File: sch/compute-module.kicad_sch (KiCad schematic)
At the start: 10 parts, among them J2 SAM10346-ND, J3 Conn_02x20_Odd_Even, M1 ComputeModule5-CM5, SW1 1825910-6

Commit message: pågebynt merging av pwr-supply og modem branches
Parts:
- renumbered C18 to C3, C19 to C4, C17 to C5, D5 to D1, J2 to J3, J3 to J4
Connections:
- net +3V3 is gone; now on net +3V3_CM5: J4.1 (Pin_1)
- net PCIE_nCLKREQ: now reaches M1.102 (PCIe_nCLKREQ)
- net PCIE_nWAKE: now reaches M1.104 (PCIE_nWAKE)
- net PCIE_PWR_EN: now reaches M1.106 (PCIE_PWR_EN)
- net PCIE_nRST: now reaches M1.109 (PCIe_nRST)
- net PCIE_CLK_P: now reaches M1.110 (PCIe_CLK_P)
- net PCIE_CLK_N: now reaches M1.112 (PCIe_CLK_N)
- net PCIE_RX_P: now reaches M1.116 (PCIe_RX_P)
- net PCIE_RX_N: now reaches M1.118 (PCIe_RX_N)
- net PCIE_TX_P: now reaches M1.122 (PCIe_TX_P)
- net PCIE_TX_N: now reaches M1.124 (PCIe_TX_N)
- no-connect marks 119 -> 109
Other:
- note added: "FLASH / BMS USB"
- note added: "MODEM USB"
- note added: "SD USB"
- moved on the sheet: BT1, C3, C4, C5, D1, J3, J4, R2, SW1

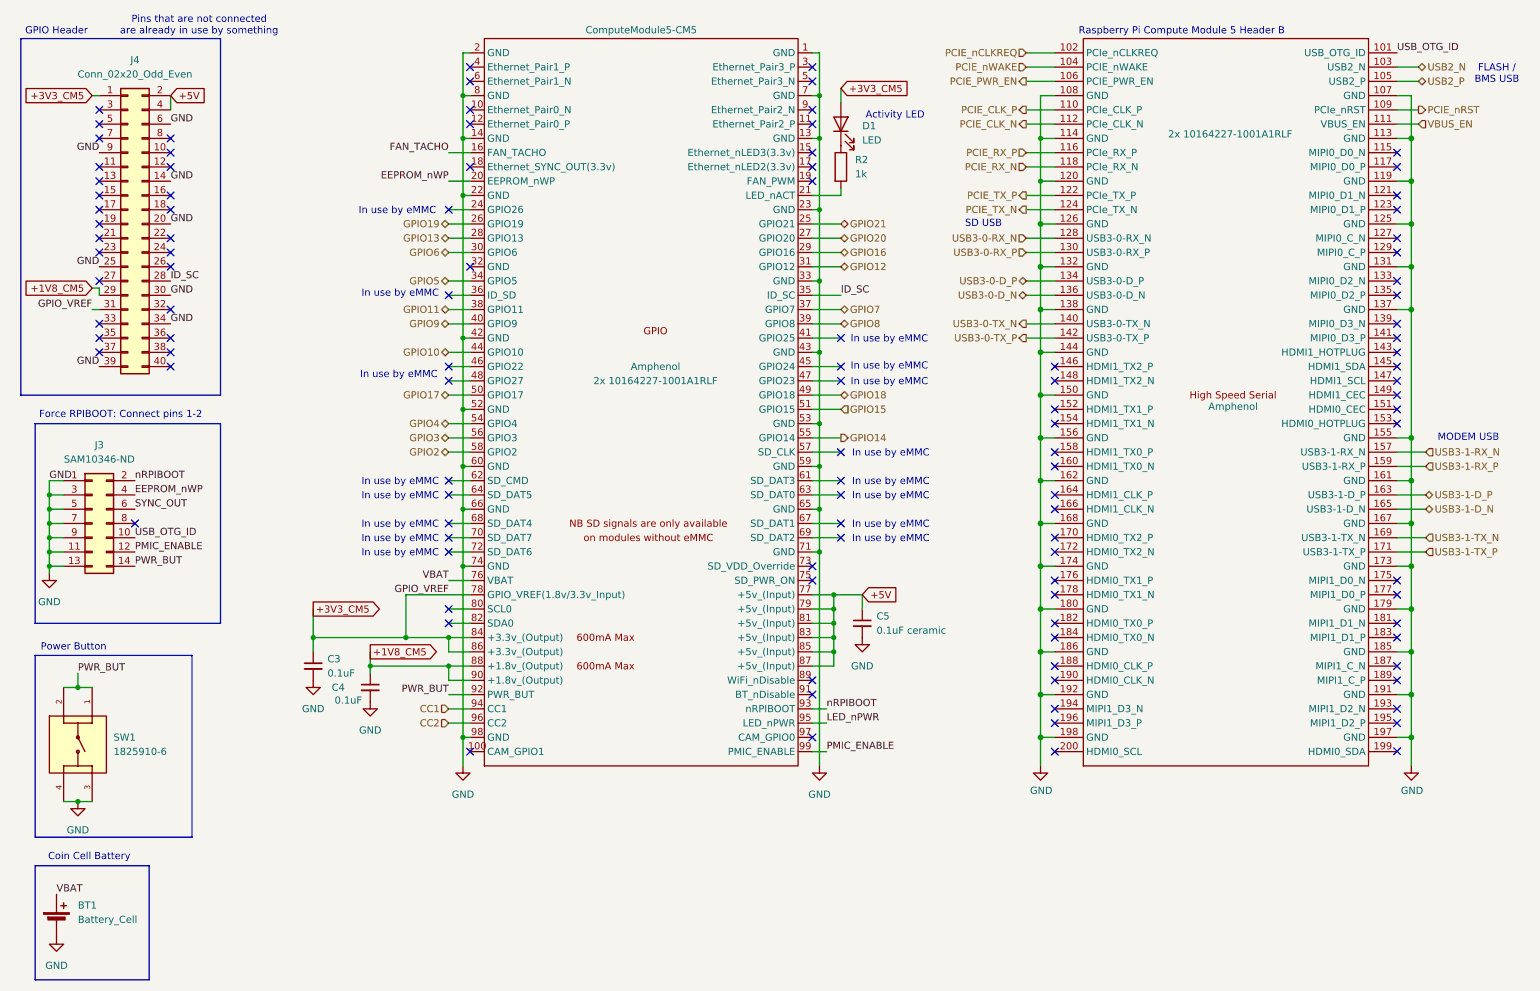
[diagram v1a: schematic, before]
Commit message: lagt inn footprint på alt, obs feil footprint i pwr-supply
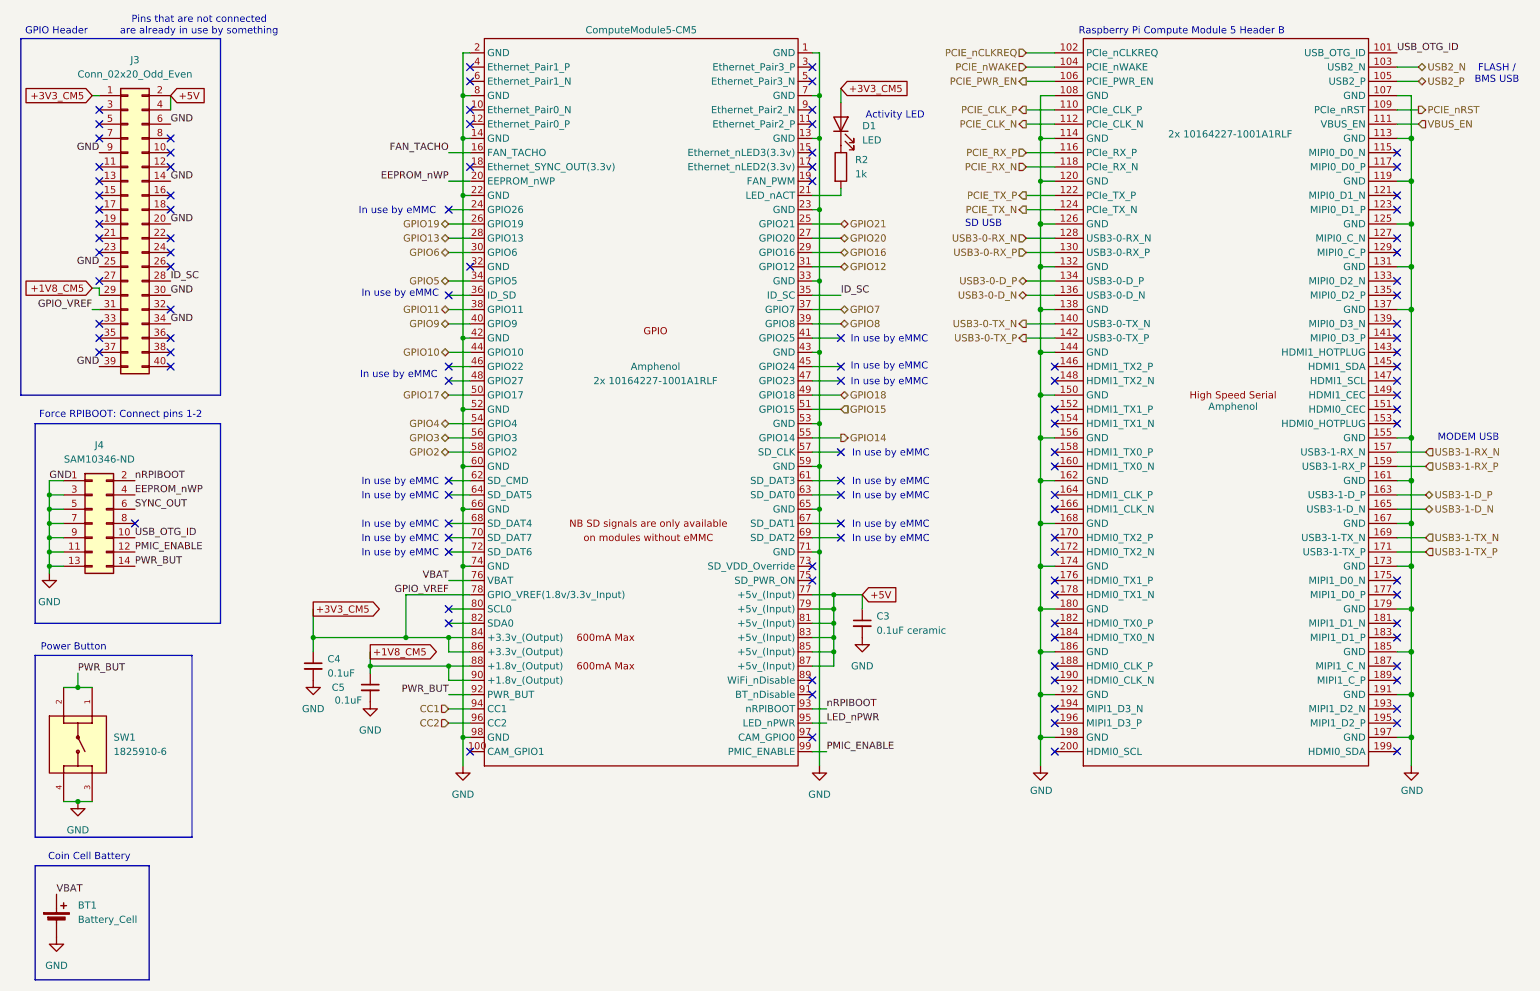
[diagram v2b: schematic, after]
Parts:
- renumbered C5 to C3, C3 to C4, C4 to C5, J4 to J3, J3 to J4
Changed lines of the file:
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@@
 		(on_board yes)
 		(dnp no)
-		(property "Reference" "#PWR017"
+		(property "Reference" "#PWR015"
 			(at 264.16 158.75 0)
 			(effects
@@
 			(project "audiograb"
 				(path "/c46c2311-6d4b-411d-b012-c7730eac136d/980eb6bd-3c2d-40a6-a375-772dc2df4153"
-					(reference "#PWR017")
+					(reference "#PWR015")
 					(unit 1)
 				)
@@
 		(on_board yes)
 		(dnp no)
-		(property "Reference" "#PWR016"
+		(property "Reference" "#PWR014"
 			(at 198.12 158.75 0)
 			(effects
@@
 			(project "audiograb"
 				(path "/c46c2311-6d4b-411d-b012-c7730eac136d/980eb6bd-3c2d-40a6-a375-772dc2df4153"
-					(reference "#PWR016")
+					(reference "#PWR014")
 					(unit 1)
 				)
@@
 		(dnp no)
 		(fields_autoplaced yes)
-		(property "Reference" "#PWR015"
+		(property "Reference" "#PWR09"
 			(at 166.37 135.89 0)
 			(effects
@@
 			(project "audiograb"
 				(path "/c46c2311-6d4b-411d-b012-c7730eac136d/980eb6bd-3c2d-40a6-a375-772dc2df4153"
-					(reference "#PWR015")
+					(reference "#PWR09")
 					(unit 1)
 				)
@@
 		(dnp no)
 		(fields_autoplaced yes)
-		(property "Reference" "J4"
+		(property "Reference" "J3"
 			(at 36.83 26.67 0)
 			(effects
@@
 			(project "audiograb"
 				(path "/c46c2311-6d4b-411d-b012-c7730eac136d/980eb6bd-3c2d-40a6-a375-772dc2df4153"
-					(reference "J4")
+					(reference "J3")
 					(unit 1)
 				)
@@
 		(on_board yes)
 		(dnp no)
-		(property "Reference" "#PWR013"
+		(property "Reference" "#PWR012"
 			(at 95.25 158.75 0)
 			(effects
@@
 			(project "audiograb"
 				(path "/c46c2311-6d4b-411d-b012-c7730eac136d/980eb6bd-3c2d-40a6-a375-772dc2df4153"
-					(reference "#PWR013")
+					(reference "#PWR012")
 					(unit 1)
 				)
@@
 		(dnp no)
 		(fields_autoplaced yes)
-		(property "Reference" "#PWR09"
+		(property "Reference" "#PWR017"
 			(at 22.86 189.23 0)
 			(effects
@@
 			(project "audiograb"
 				(path "/c46c2311-6d4b-411d-b012-c7730eac136d/980eb6bd-3c2d-40a6-a375-772dc2df4153"
-					(reference "#PWR09")
+					(reference "#PWR017")
 					(unit 1)
 				)
@@
 		(dnp no)
 		(fields_autoplaced yes)
-		(property "Reference" "#PWR011"
+		(property "Reference" "#PWR010"
 			(at 68.58 143.51 0)
 			(effects
@@
 			(project "audiograb"
 				(path "/c46c2311-6d4b-411d-b012-c7730eac136d/980eb6bd-3c2d-40a6-a375-772dc2df4153"
-					(reference "#PWR011")
+					(reference "#PWR010")
 					(unit 1)
 				)
@@
 		(dnp no)
 		(fields_autoplaced yes)
-		(property "Reference" "C3"
+		(property "Reference" "C4"
 			(at 71.12 133.3562 0)
 			(effects
@@
 			(project "audiograb"
 				(path "/c46c2311-6d4b-411d-b012-c7730eac136d/980eb6bd-3c2d-40a6-a375-772dc2df4153"
-					(reference "C3")
+					(reference "C4")
 					(unit 1)
 				)
@@
 		(dnp no)
 		(fields_autoplaced yes)
-		(property "Reference" "#PWR012"
+		(property "Reference" "#PWR011"
 			(at 78.74 147.32 0)
 			(effects
@@
 			(project "audiograb"
 				(path "/c46c2311-6d4b-411d-b012-c7730eac136d/980eb6bd-3c2d-40a6-a375-772dc2df4153"
-					(reference "#PWR012")
+					(reference "#PWR011")
 					(unit 1)
 				)
@@
 		(dnp no)
 		(fields_autoplaced yes)
-		(property "Reference" "C5"
+		(property "Reference" "C3"
 			(at 168.91 125.7362 0)
 			(effects
@@
 			(project "audiograb"
 				(path "/c46c2311-6d4b-411d-b012-c7730eac136d/980eb6bd-3c2d-40a6-a375-772dc2df4153"
-					(reference "C5")
+					(reference "C3")
 					(unit 1)
 				)
@@
 		(dnp no)
 		(fields_autoplaced yes)
-		(property "Reference" "J3"
+		(property "Reference" "J4"
 			(at 30.48 95.25 0)
 			(effects
@@
 			(project "audiograb"
 				(path "/c46c2311-6d4b-411d-b012-c7730eac136d/980eb6bd-3c2d-40a6-a375-772dc2df4153"
-					(reference "J3")
+					(reference "J4")
 					(unit 1)
 				)
@@
 		(dnp no)
 		(fields_autoplaced yes)
-		(property "Reference" "#PWR014"
+		(property "Reference" "#PWR013"
 			(at 158.75 158.75 0)
 			(effects
@@
 			(project "audiograb"
 				(path "/c46c2311-6d4b-411d-b012-c7730eac136d/980eb6bd-3c2d-40a6-a375-772dc2df4153"
-					(reference "#PWR014")
+					(reference "#PWR013")
 					(unit 1)
 				)
@@
 		(dnp no)
 		(fields_autoplaced yes)
-		(property "Reference" "#PWR010"
+		(property "Reference" "#PWR016"
 			(at 26.67 165.1 0)
 			(effects
@@
 			(project "audiograb"
 				(path "/c46c2311-6d4b-411d-b012-c7730eac136d/980eb6bd-3c2d-40a6-a375-772dc2df4153"
-					(reference "#PWR010")
+					(reference "#PWR016")
 					(unit 1)
 				)
@@
 		(on_board yes)
 		(dnp no)
-		(property "Reference" "C4"
+		(property "Reference" "C5"
 			(at 71.882 138.43 0)
 			(effects
@@
 			(project "audiograb"
 				(path "/c46c2311-6d4b-411d-b012-c7730eac136d/980eb6bd-3c2d-40a6-a375-772dc2df4153"
-					(reference "C4")
+					(reference "C5")
 					(unit 1)
 				)

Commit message: Fjernet gammelt og la til nye komponenter, merging ferdig
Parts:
- removed BT1: Battery_Cell, Battery:BatteryHolder_Keystone_3034_1x20mm, symbol Device:Battery_Cell
- renumbered C3 to C17, C4 to C18, C5 to C19, D1 to D5, J4 to J2
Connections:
- net VBAT is gone; now on net +3V3_CM5: M1.76 (VBAT)
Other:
- note removed: "Coin Cell Battery"
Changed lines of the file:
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@@
 		)
 	)
-	(rectangle
-		(start 19.05 170.18)
-		(end 39.37 190.5)
-		(stroke
-			(width 0)
-			(type default)
-		)
-		(fill
-			(type none)
-		)
-	)
 	(text "In use by eMMC"
 		(exclude_from_sim no)
@@
 		)
 	)
-	(text "Coin Cell Battery"
-		(exclude_from_sim no)
-		(at 28.702 168.656 0)
-		(effects
-			(font
-				(size 1.27 1.27)
-			)
-		)
-	)
 	(text "Power Button\n"
 		(exclude_from_sim no)
@@
 	(wire
 		(pts
+			(xy 93.98 119.38) (xy 96.52 119.38)
+		)
+		(stroke
+			(width 0)
+			(type default)
+		)
+	)
+	(wire
+		(pts
 			(xy 198.12 109.22) (xy 198.12 116.84)
 		)
@@
 	(wire
 		(pts
+			(xy 93.98 118.11) (xy 93.98 119.38)
+		)
+		(stroke
+			(width 0)
+			(type default)
+		)
+	)
+	(wire
+		(pts
 			(xy 264.16 147.32) (xy 264.16 152.4)
 		)
@@
 	(wire
 		(pts
-			(xy 92.71 119.38) (xy 96.52 119.38)
+			(xy 90.17 118.11) (xy 93.98 118.11)
 		)
 		(stroke
@@
 		)
 	)
-	(label "VBAT"
-		(at 92.71 119.38 180)
-		(effects
-			(font
-				(size 1.27 1.27)
-			)
-			(justify right bottom)
-		)
-	)
 	(label "PMIC_ENABLE"
 		(at 36.83 114.3 0)
@@
 		)
 	)
-	(label "VBAT"
-		(at 22.86 175.26 0)
-		(effects
-			(font
-				(size 1.27 1.27)
-			)
-			(justify left bottom)
-		)
-	)
 	(label "GPIO_VREF"
 		(at 29.21 71.12 180)
@@
 	)
 	(global_label "+3V3_CM5"
+		(shape input)
+		(at 90.17 118.11 180)
+		(fields_autoplaced yes)
+		(effects
+			(font
+				(size 1.27 1.27)
+			)
+			(justify right)
+		)
+		(property "Intersheetrefs" "${INTERSHEET_REFS}"
+			(at 82.1048 118.11 0)
+			(effects
+				(font
+					(size 1.27 1.27)
+				)
+				(justify right)
+				(hide yes)
+			)
+		)
+	)
+	(global_label "+3V3_CM5"
 		(shape output)
 		(at 68.58 124.46 0)
@@
 	(symbol
 		(lib_id "power:GND")
-		(at 22.86 182.88 0)
-		(unit 1)
-		(exclude_from_sim no)
-		(in_bom yes)
-		(on_board yes)
-		(dnp no)
-		(fields_autoplaced yes)
-		(property "Reference" "#PWR017"
-			(at 22.86 189.23 0)
-			(effects
-				(font
-					(size 1.27 1.27)
-				)
-				(hide yes)
-			)
-		)
-		(property "Value" "GND"
-			(at 22.86 187.96 0)
-			(effects
-				(font
-					(size 1.27 1.27)
-				)
-			)
-		)
-		(property "Footprint" ""
-			(at 22.86 182.88 0)
-			(effects
-				(font
-					(size 1.27 1.27)
-				)
-				(hide yes)
-			)
-		)
-		(property "Datasheet" ""
-			(at 22.86 182.88 0)
-			(effects
-				(font
-					(size 1.27 1.27)
-				)
-				(hide yes)
-			)
-		)
-		(property "Description" "Power symbol creates a global label with name \"GND\" , ground"
-			(at 22.86 182.88 0)
-			(effects
-				(font
-					(size 1.27 1.27)
-				)
-				(hide yes)
-			)
-		)
-		(pin "1"
-		)
-		(instances
-			(project "audiograb"
-				(path "/c46c2311-6d4b-411d-b012-c7730eac136d/980eb6bd-3c2d-40a6-a375-772dc2df4153"
-					(reference "#PWR017")
-					(unit 1)
-				)
-			)
-		)
-	)
-	(symbol
-		(lib_id "power:GND")
 		(at 68.58 137.16 0)
 		(unit 1)
@@
 		(dnp no)
 		(fields_autoplaced yes)
-		(property "Reference" "C4"
+		(property "Reference" "C18"
 			(at 71.12 133.3562 0)
 			(effects
@@
 			(project "audiograb"
 				(path "/c46c2311-6d4b-411d-b012-c7730eac136d/980eb6bd-3c2d-40a6-a375-772dc2df4153"
-					(reference "C4")
+					(reference "C18")
 					(unit 1)
 				)
@@
 		(dnp no)
 		(fields_autoplaced yes)
-		(property "Reference" "C3"
+		(property "Reference" "C17"
 			(at 168.91 125.7362 0)
 			(effects
@@
 			(project "audiograb"
 				(path "/c46c2311-6d4b-411d-b012-c7730eac136d/980eb6bd-3c2d-40a6-a375-772dc2df4153"
-					(reference "C3")
+					(reference "C17")
 					(unit 1)
 				)
@@
 		(dnp no)
 		(fields_autoplaced yes)
-		(property "Reference" "J4"
+		(property "Reference" "J2"
 			(at 30.48 95.25 0)
 			(effects
@@
 			(project "audiograb"
 				(path "/c46c2311-6d4b-411d-b012-c7730eac136d/980eb6bd-3c2d-40a6-a375-772dc2df4153"
-					(reference "J4")
+					(reference "J2")
 					(unit 1)
 				)
@@
 		(dnp no)
 		(fields_autoplaced yes)
-		(property "Reference" "D1"
+		(property "Reference" "D5"
 			(at 166.37 38.4174 90)
 			(effects
@@
 			(project "audiograb"
 				(path "/c46c2311-6d4b-411d-b012-c7730eac136d/980eb6bd-3c2d-40a6-a375-772dc2df4153"
-					(reference "D1")
+					(reference "D5")
 					(unit 1)
 				)
@@
 	)
 	(symbol
-		(lib_id "Device:Battery_Cell")
-		(at 22.86 180.34 0)
-		(unit 1)
-		(exclude_from_sim no)
-		(in_bom yes)
-		(on_board yes)
-		(dnp no)
-		(fields_autoplaced yes)
-		(property "Reference" "BT1"
-			(at 26.67 177.2284 0)
-			(effects
-				(font
-					(size 1.27 1.27)
-				)
-				(justify left)
-			)
-		)
-		(property "Value" "Battery_Cell"
-			(at 26.67 179.7684 0)
-			(effects
-				(font
-					(size 1.27 1.27)
-				)
-				(justify left)
-			)
-		)
-		(property "Footprint" "Battery:BatteryHolder_Keystone_3034_1x20mm"
-			(at 22.86 178.816 90)
-			(effects
-				(font
-					(size 1.27 1.27)
-				)
-				(hide yes)
-			)
-		)
-		(property "Datasheet" "~"
-			(at 22.86 178.816 90)
-			(effects
-				(font
-					(size 1.27 1.27)
-				)
-				(hide yes)
-			)
-		)
-		(property "Description" "Single-cell battery"
-			(at 22.86 180.34 0)
-			(effects
-				(font
-					(size 1.27 1.27)
-				)
-				(hide yes)
-			)
-		)
-		(property "Sim.Device" "V"
-			(at 22.86 180.34 0)
-			(effects
-				(font
-					(size 1.27 1.27)
-				)
-				(hide yes)
-			)
-		)
-		(property "Sim.Type" "DC"
-			(at 22.86 180.34 0)
-			(effects
-				(font
-					(size 1.27 1.27)
-				)
-				(hide yes)
-			)
-		)
-		(property "Sim.Pins" "1=+ 2=-"
-			(at 22.86 180.34 0)
-			(effects
-				(font
-					(size 1.27 1.27)
-				)
-				(hide yes)
-			)
-		)
-		(pin "1"
-		)
-		(pin "2"
-		)
-		(instances
-			(project "audiograb"
-				(path "/c46c2311-6d4b-411d-b012-c7730eac136d/980eb6bd-3c2d-40a6-a375-772dc2df4153"
-					(reference "BT1")
-					(unit 1)
-				)
-			)
-		)
-	)
-	(symbol
 		(lib_id "CM5IO:ComputeModule5-CM5")
 		(at 91.44 86.36 0)
@@
 		(on_board yes)
 		(dnp no)
-		(property "Reference" "C5"
+		(property "Reference" "C19"
 			(at 71.882 138.43 0)
 			(effects
@@
 			(project "audiograb"
 				(path "/c46c2311-6d4b-411d-b012-c7730eac136d/980eb6bd-3c2d-40a6-a375-772dc2df4153"
-					(reference "C5")
+					(reference "C19")
 					(unit 1)
 				)

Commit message: Routa SD-lytte på cm på nytt
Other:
- note added: "SD2"
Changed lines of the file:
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@@
+		)
+	)
+	(text "SD2"
+		(exclude_from_sim no)
+		(at 173.482 86.614 0)
+		(effects
+			(font
+				(size 1.27 1.27)
+			)
 		)
 	)
